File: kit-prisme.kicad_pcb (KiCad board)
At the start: 2 copper layers, 175.5 x 126.5 mm, 120 parts, among them J1 Conn_01x02, J10 Conn_01x03, J11 Conn_01x04, J12 Conn_01x04, J13 Conn_01x04, J14 Conn_01x04, J15 Conn_01x04, J16 Conn_01x04, J17 Conn_01x04, J18 Conn_01x04, J19 Conn_01x04, J2 Conn_01x16, J20 Conn_01x04, J21 Conn_01x04, J22 Conn_01x04, J23 Conn_01x04, J24 Conn_01x04, J25 Conn_01x04, J26 Conn_01x04, J3 Conn_01x16, J4 Conn_01x16, J5 Conn_01x02, J6 Conn_01x02, J7 Conn_01x04, J8 Conn_01x04, J9 Conn_01x04, Q1 2N7000, Q10 2N7000, Q11 2N7000, Q2 2N7000, Q3 2N7000, Q4 2N7000, Q5 2N7000, Q6 2N7000, Q7 2N7000, Q8 2N7000, Q9 2N7000

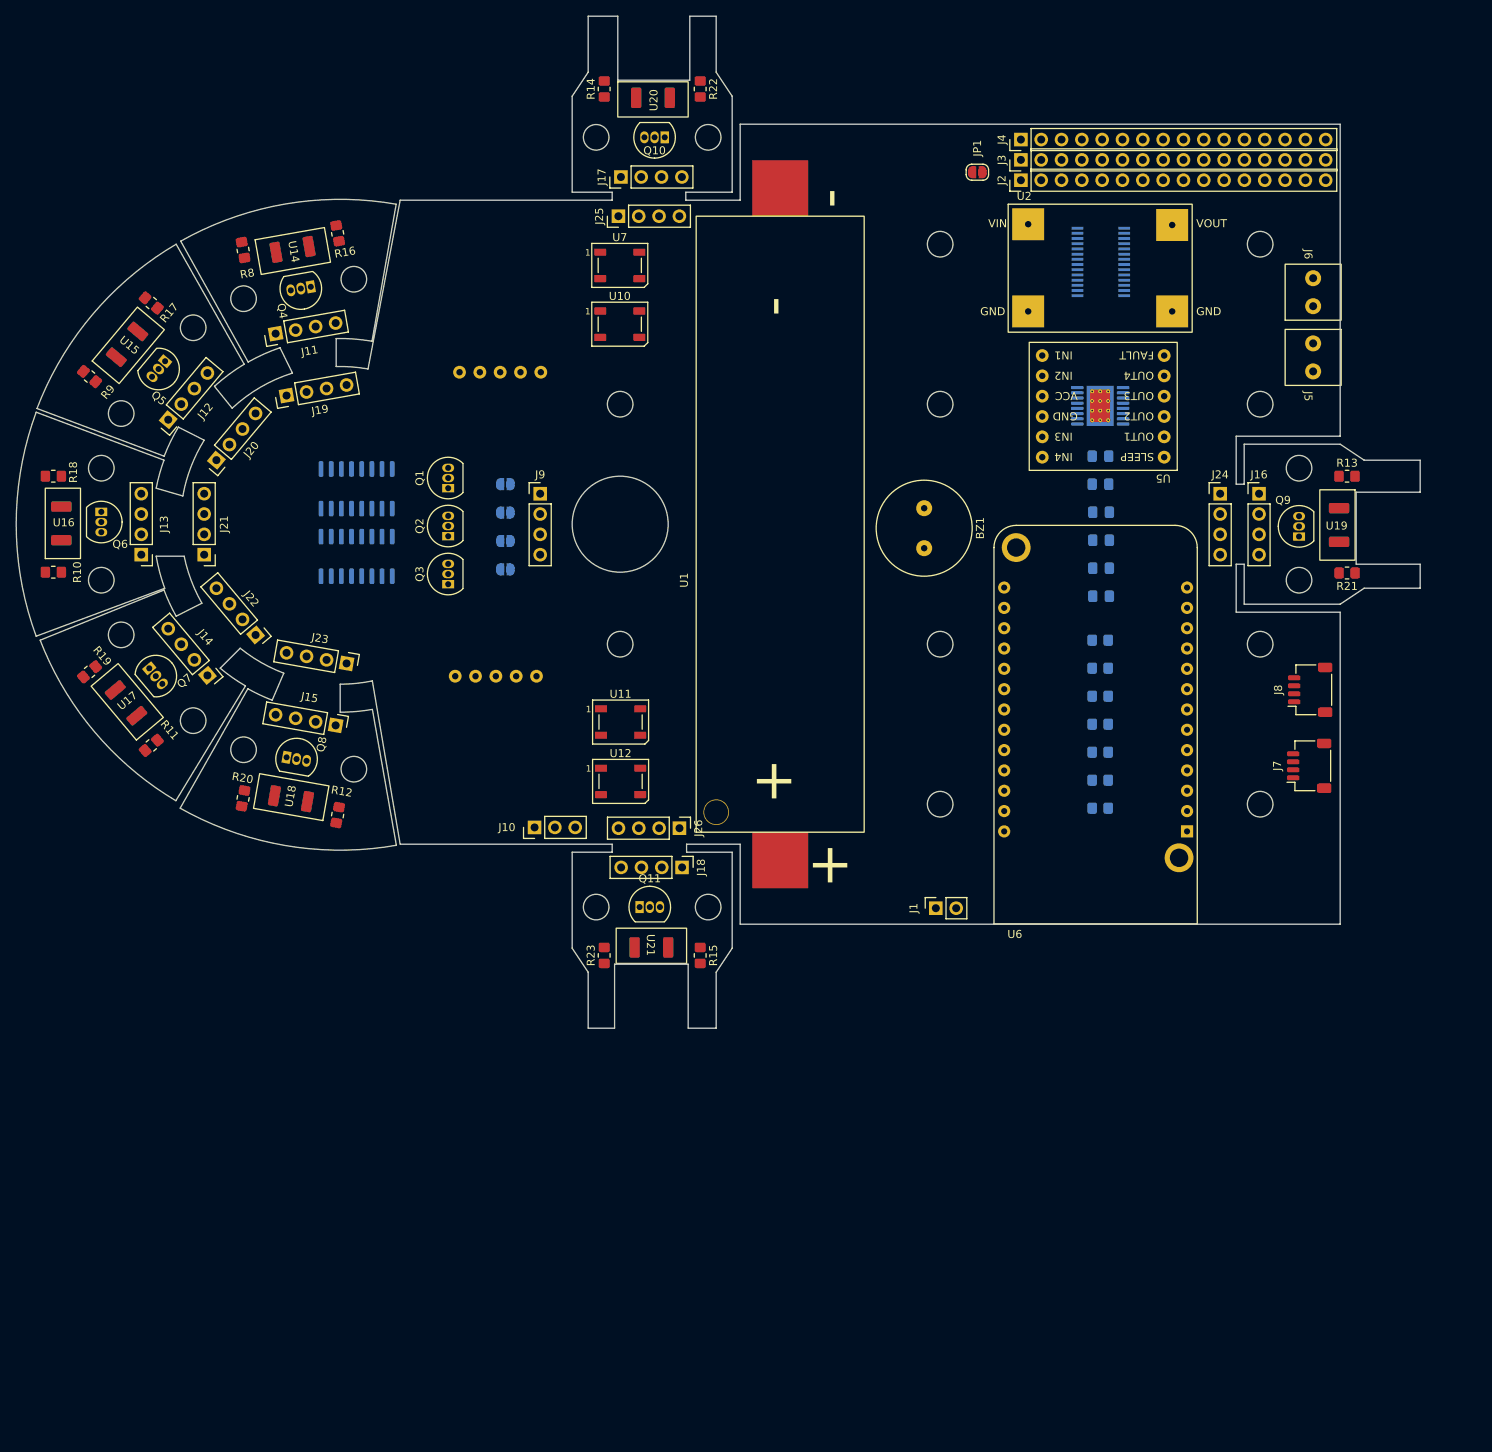
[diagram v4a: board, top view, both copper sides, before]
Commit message: redit bouard edge cut, shrinked a bit the board
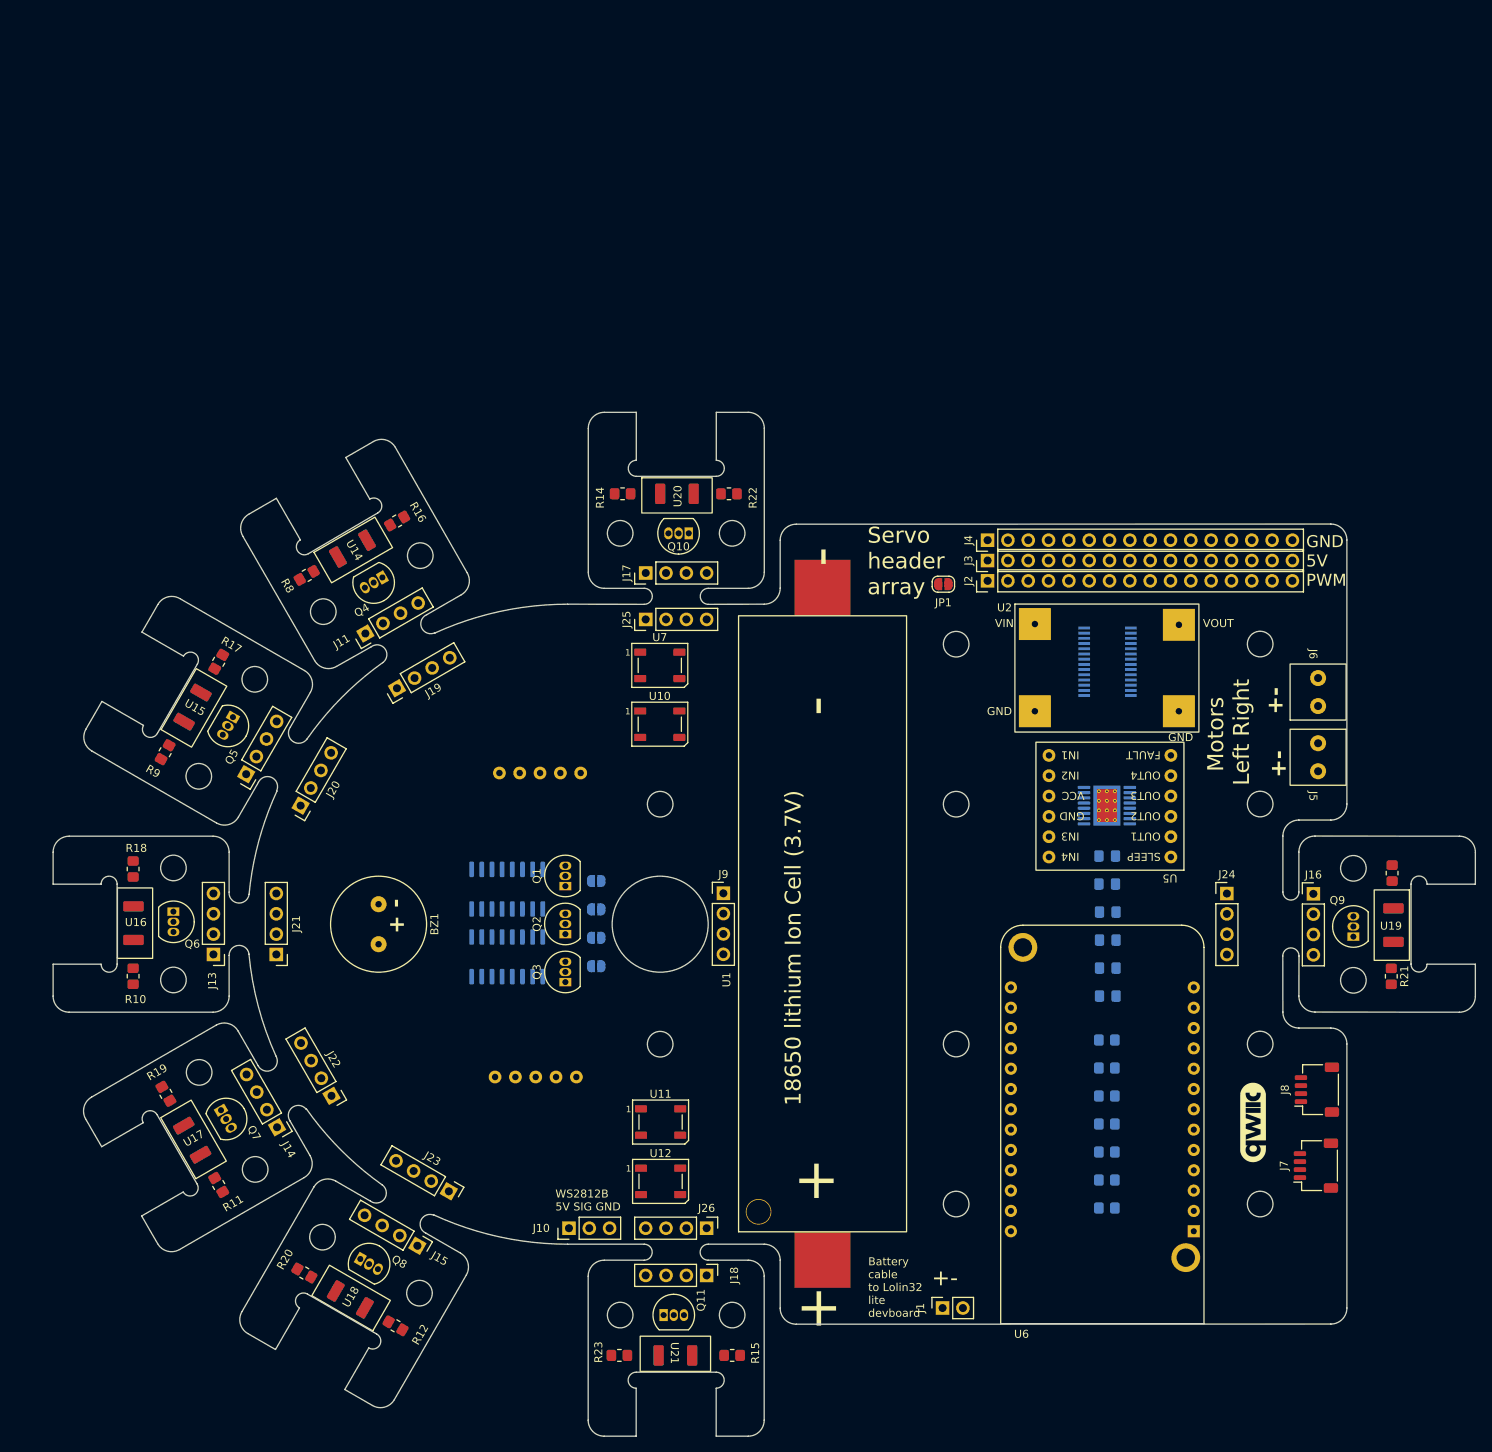
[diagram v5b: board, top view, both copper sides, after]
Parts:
- added G***: LOGO, kit-prisme:qwiic_10mm, F.Cu at (264.1, 174.8)
- moved BZ1 84.3 mm to (154.8, 150.0)
- moved J23 67.2 mm to (163.6, 183.4), turned to -120 degrees
- moved REF**7 66.0 mm to (159.9, 196.1), turned to 150 degrees
- moved J15 65.8 mm to (159.7, 190.2), turned to -120 degrees
- moved R12 64.3 mm to (156.9, 200.2), turned to 150 degrees
- moved Q8 63.4 mm to (152.5, 191.8), turned to -30 degrees
- moved U18 63.0 mm to (151.3, 196.9), turned to 150 degrees
- moved REF**8 61.7 mm to (147.8, 189.1), turned to 150 degrees
- moved R20 59.8 mm to (145.5, 193.6), turned to 150 degrees
- moved J22 58.4 mm to (148.9, 171.5), turned to -150 degrees
- moved J14 57.2 mm to (142.1, 175.4), turned to -150 degrees
- moved REF**5 56.6 mm to (139.4, 180.6), turned to 120 degrees
- moved Q7 56.0 mm to (135.1, 173.3), turned to -60 degrees
- moved R11 55.6 mm to (134.8, 182.6), turned to -60 degrees
- moved REF**6 55.6 mm to (132.4, 168.5), turned to 120 degrees
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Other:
- board size 175.5 x 126.5 mm -> 177.8 x 128 mm
- board text added: "+-"
- board text added: "- +"
- board text added: "18650 lithium Ion Cell (3.7V)"
- board text added: "6mm width, 1.6mm thickness, lever lenght : 22mm The IR sensor should break with force between 10 N and 70 N (1-7Kg)"
- board text added: "Battery cable to Lolin32 lite devboard"
- board text added: "Could the PCB have been smaller ? sure would it be as easy to solder ? not so sure"
- board text added: "GND 5V PWM"
- board text added: "Motors Left Right"
- board text added: "Radius and groove are based on a typical PCB drill (2mm diameter, 1mm radius"
- board text added: "Servo header array"
- board text added: "WS2812B 5V SIG GND"
- board text added: "each IR sensor can be broken and reconnected using four cable at a different location"
- board text added: "its a IR for line following for instance"
- board text added: "theses are made to be broken off and soldered unsing 90° pin header bellow the PCB"
- board text added: "this allow you to change the mechanical layout or use other (analog) sensors if you want to repurpose the kit"

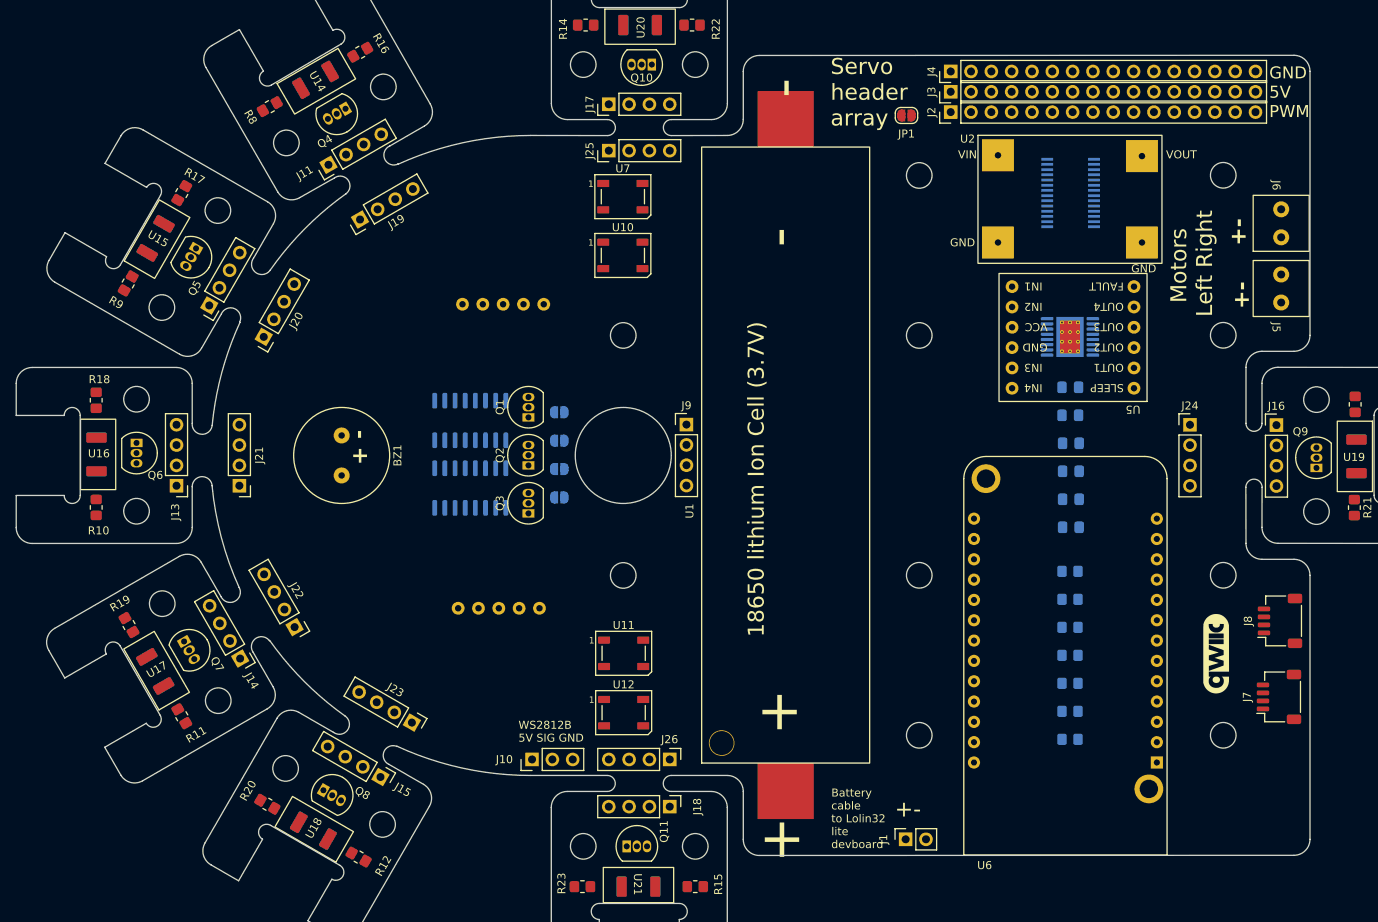
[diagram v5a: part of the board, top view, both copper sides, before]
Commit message: improved silkscreen
added instruction and naming of component
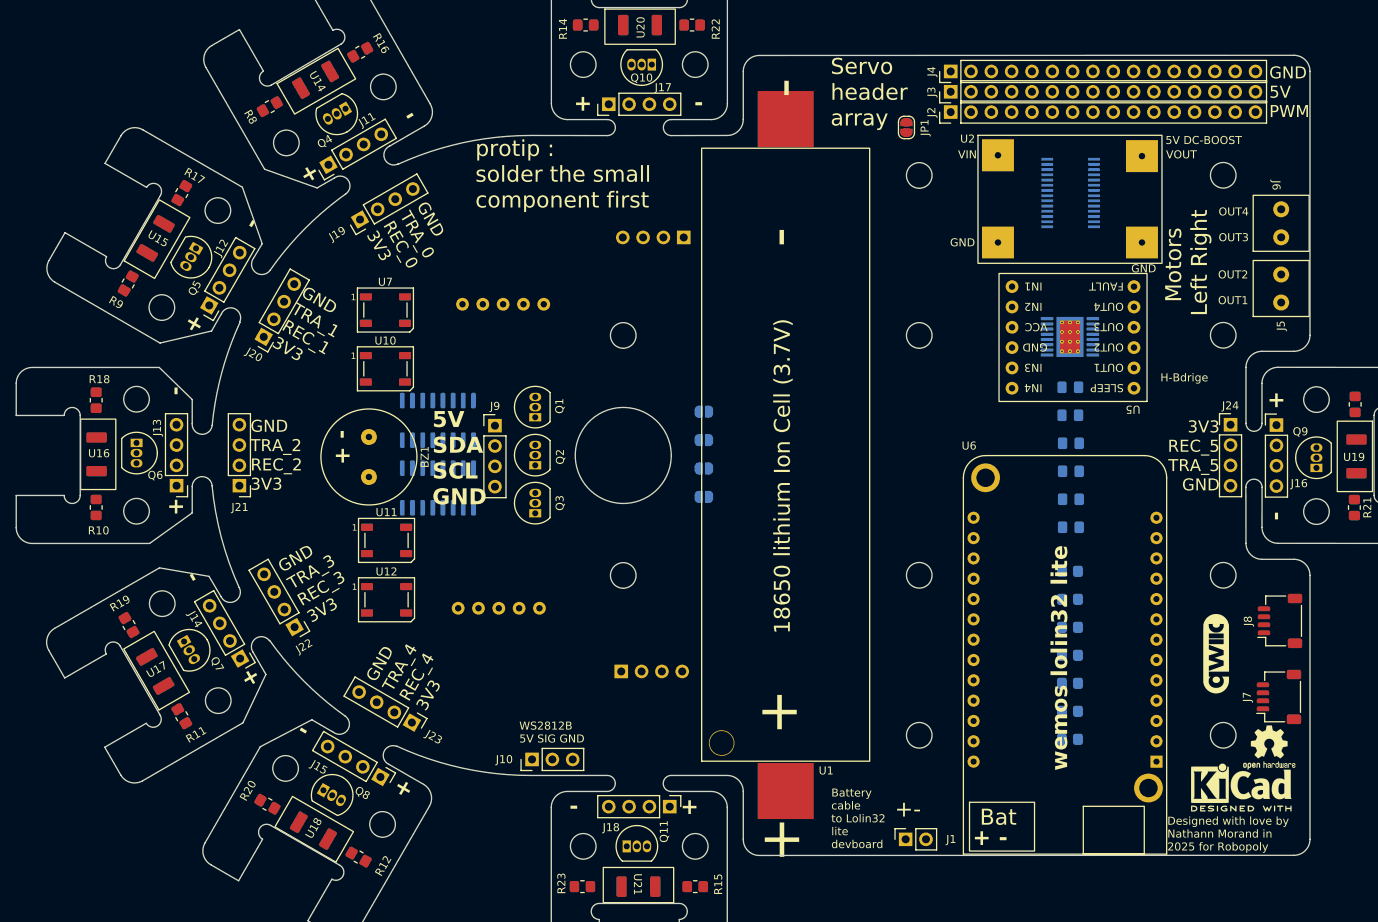
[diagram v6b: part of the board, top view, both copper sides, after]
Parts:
- added G***: LOGO, kit-prisme:RobopolyLogo, B.Cu at (211.5, 121.5)
- added REF**: KiCad-Logo2_5mm_SilkScreen, Symbol:KiCad-Logo2_5mm_SilkScreen, F.Cu at (267.2, 191.5)
- added REF**: OSHW-Logo2_7.3x6mm_SilkScreen, Symbol:OSHW-Logo2_7.3x6mm_SilkScreen, F.Cu at (270.8, 186.5)
- J25, J26: moved to B.Cu
- moved U10 32.9 mm to (160.3, 139.2)
- moved U7 32.9 mm to (160.3, 131.8)
- moved U12 32.8 mm to (160.4, 168.0)
- moved U11 32.8 mm to (160.4, 160.6)
- moved J9 23.9 mm to (174.0, 146.3)
- moved JP2 18.1 mm to (200.1, 144.5)
- moved JP3 18.1 mm to (200.1, 148.1)
- moved JP4 18.1 mm to (200.1, 151.6)
- moved JP5 18.1 mm to (200.1, 155.2)
- moved J25 14.3 mm to (197.6, 122.8)
- moved J26 12.6 mm to (189.8, 177.0)
- moved J24 5.07 mm to (265.9, 146.2)
- moved U13 4.05 mm to (166.8, 154.1)
- moved U22 4.05 mm to (166.8, 145.6)
- moved BZ1 3.42 mm to (158.2, 150.2)
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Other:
- outline, holes or cut-outs redrawn
- board text added: "+"
- board text added: "-"
- board text added: "3V3 REC_5 TRA_5 GND"
- board text added: "5V DC-BOOST"
- board text added: "5V SDA SCL GND"
- board text added: "Designed with love by Nathann Morand in 2025 for Robopoly"
- board text added: "Do not solder a chip here before removing the h-bridge module. This is intended for User looking for a greater soldering challenge :)"
- board text added: "GND TRA_0 REC_0 3V3"
- board text added: "GND TRA_1 REC_1 3V3"
- board text added: "GND TRA_2 REC_2 3V3"
- board text added: "GND TRA_3 REC_3 3V3"
- board text added: "GND TRA_4 REC_4 3V3"
- board text added: "GND TRA_6 REC_6 3V3"
- board text added: "GND TRA_7 REC_7 3V3"
- board text added: "H-Bdrige"
- board text added: "Kit Prisme New This pcb is a small wheeled robot that aimed to be a introductory project involving soldering and applied robotics. Have fun"
- board text added: "OUT2 OUT1"
- board text added: "OUT4 OUT3"
- board text added: "Rotary Encoder They also serve as wheel axis"
- board text added: "bottom IR sensor. Point toward the ground"
- board text added: "led / Servo PWM driver"
- board text added: "protip : solder the small component first"

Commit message: routed the PCB
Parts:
- moved J25 7.81 mm to (189.8, 123.0), turned to -90 degrees
- moved J26 7.50 mm to (197.2, 177.0), turned to 90 degrees
- moved Q1 2.61 mm to (181.6, 145.2)
- moved Q2 2.61 mm to (181.6, 151.2)
- moved Q3 2.61 mm to (181.6, 157.2)
- moved J9 2.61 mm to (176.6, 146.3)
- moved U22 1.37 mm to (166.8, 144.2)
- moved U13 1.20 mm to (167.0, 155.2)
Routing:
- net GND: track 0.00 -> 995.4 mm, vias 0 -> 22
- net +3V3: track 0.00 -> 863.1 mm, vias 0 -> 32
- net +5V: track 0.00 -> 384.1 mm, vias 0 -> 17
- net IR_REC_7: track 0.00 -> 202.9 mm, vias 0 -> 7
- net SDA: track 0.00 -> 195.8 mm, vias 0 -> 7
- net SCL: track 0.00 -> 188.2 mm, vias 0 -> 7
- net RE_Left_btn: track 0.00 -> 177.4 mm, vias 0 -> 2
- net IR_MODULATION: track 0.00 -> 153.4 mm, vias 0 -> 3
- net WS2812_DIN: track 0.00 -> 148.9 mm, vias 0 -> 2
- net IR_REC_5: track 0.00 -> 141.4 mm, vias 0 -> 4
- net RE_Left_A: track 0.00 -> 140.8 mm, vias 0 -> 1
- net RE_Left_B: track 0.00 -> 127.8 mm, vias 0 -> 1
- net Net-(J3-Pin_1): track 0.00 -> 127.4 mm, vias 0 -> 2
- net IR_analog: track 0.00 -> 126.3 mm, vias 0 -> 3
- net IR_TRA_5: track 0.00 -> 126.3 mm, vias 0 -> 3
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- added copper zone on F.Cu, net +3V3
- added copper zone on B.Cu, net GND
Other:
- board text added: "3V3 REC_6 TRA_6 GND"
- board text added: "3V3 REC_7 TRA_7 GND"
- board text added: "Kit Prisme New V0.0 This pcb is a small wheeled robot that aimed to be a introductory project involving soldering and applied robotics. Have fun"
- board text removed: "GND TRA_6 REC_6 3V3"
- board text removed: "GND TRA_7 REC_7 3V3"
- board text removed: "Kit Prisme New This pcb is a small wheeled robot that aimed to be a introductory project involving soldering and applied robotics. Have fun"

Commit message: assembling test version, added issue / improvment
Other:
- board text added: "ADD VCUT / dont break CLEANLY"
- board text added: "Check footprint"
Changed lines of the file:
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@@
+		)
+	)
+	(gr_text "ADD VCUT / dont break CLEANLY"
+		(at 211 90 0)
+		(layer "User.2")
+		(effects
+			(font
+				(size 1 1)
+				(thickness 0.15)
+			)
+			(justify left bottom)
+		)
+	)
+	(gr_text "Check footprint"
+		(at 167.5 169.5 0)
+		(layer "User.2")
+		(effects
+			(font
+				(size 1 1)
+				(thickness 0.15)
+			)
+			(justify left bottom)
 		)
 	)
